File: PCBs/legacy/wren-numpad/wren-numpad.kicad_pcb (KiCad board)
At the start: 2 copper layers, 227.7 x 112.8 mm, 105 parts, among them J1 TRRS_Jack, SW0 Reset, U1 Elite-C

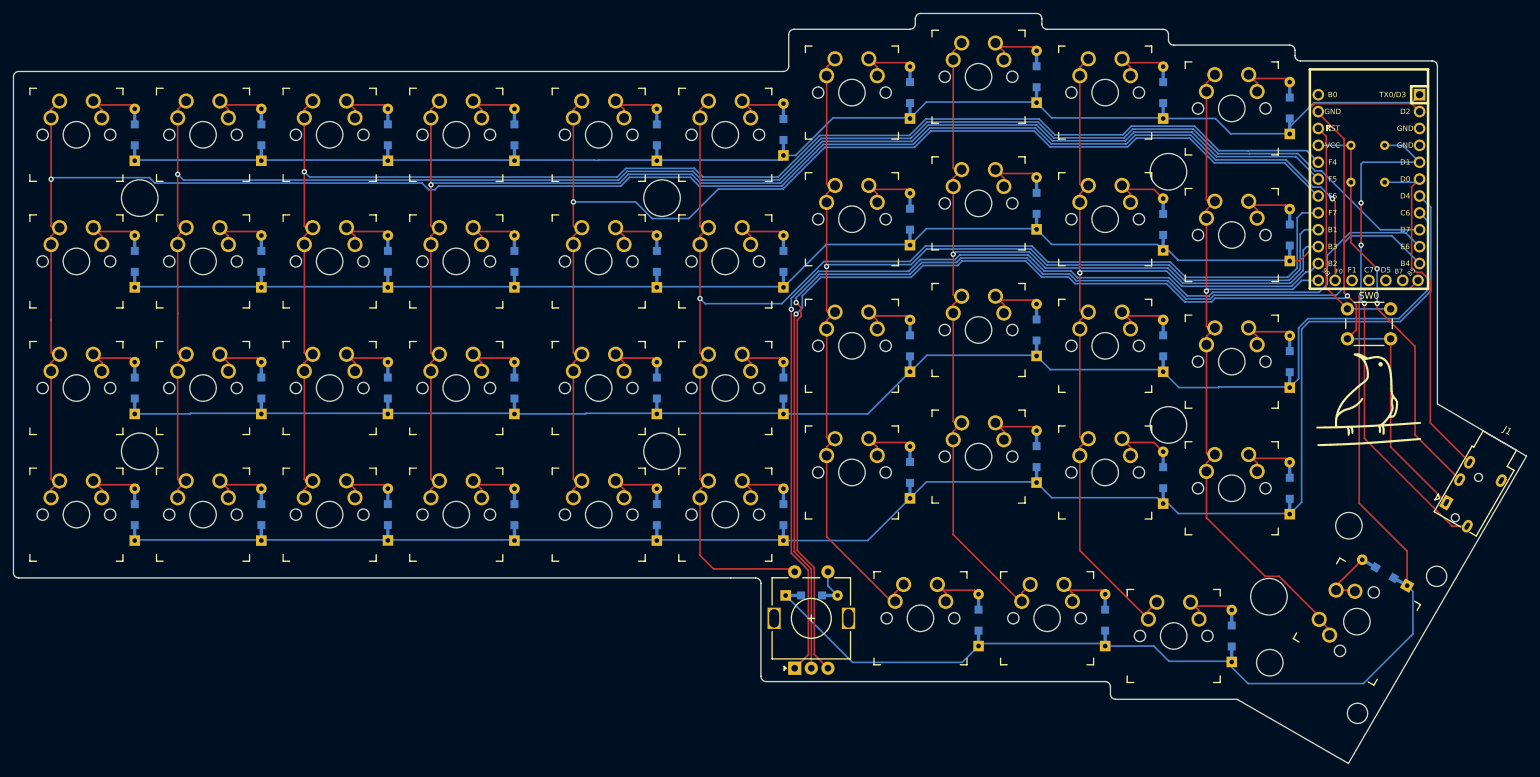
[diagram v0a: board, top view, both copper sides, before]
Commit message: Update screw positions on plates to match universal PCBs, update Gerbers
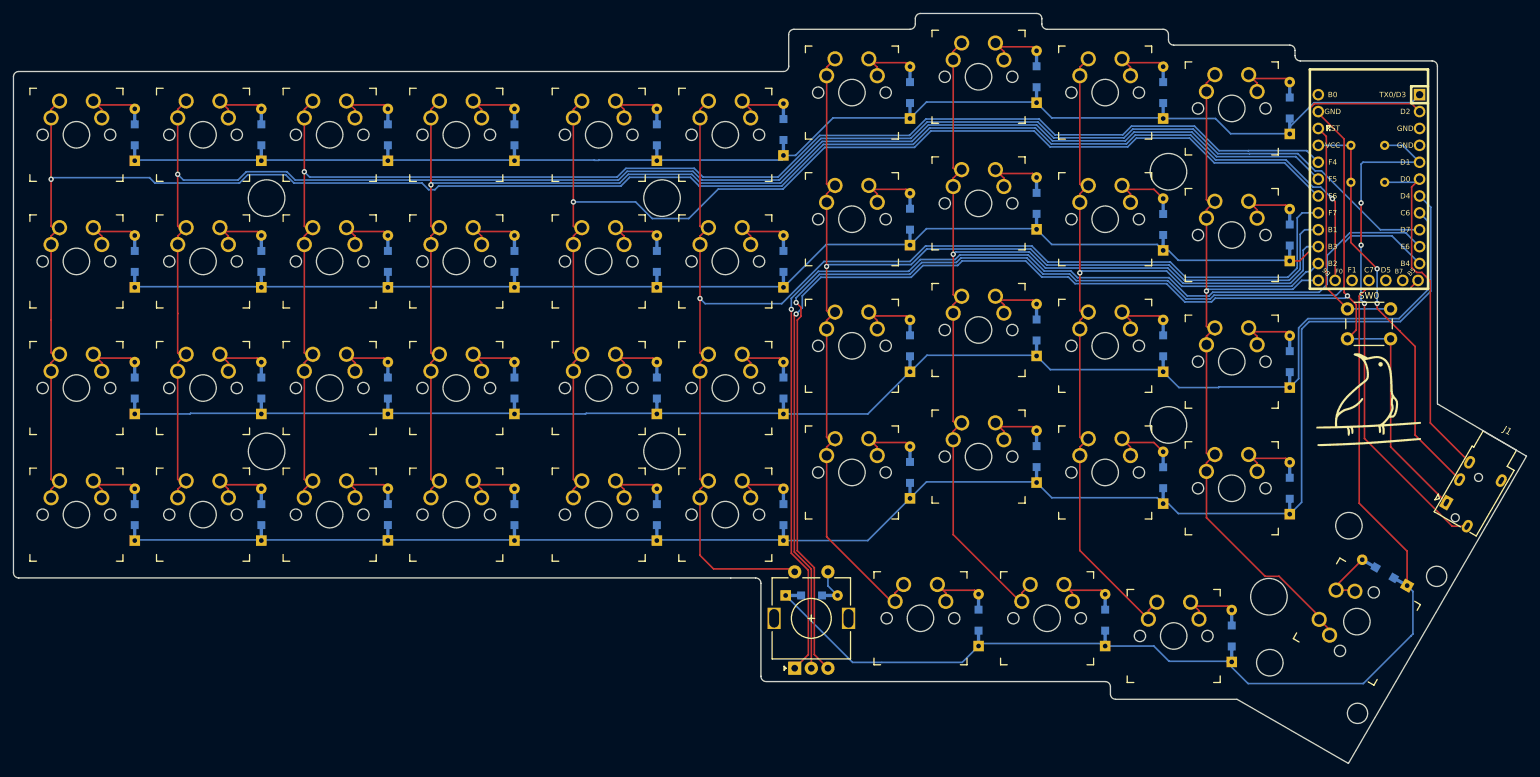
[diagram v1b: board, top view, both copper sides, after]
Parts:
- moved H1 19.1 mm to (75.4, 46.0)
- moved H4 19.1 mm to (75.4, 84.1)
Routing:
- net COL8: track 266.4 -> 267.4 mm
- net COL9: track 283.2 -> 284.2 mm
